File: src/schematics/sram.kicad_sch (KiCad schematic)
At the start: 4 parts, among them U9 IS61WV25616BLL-*BLI

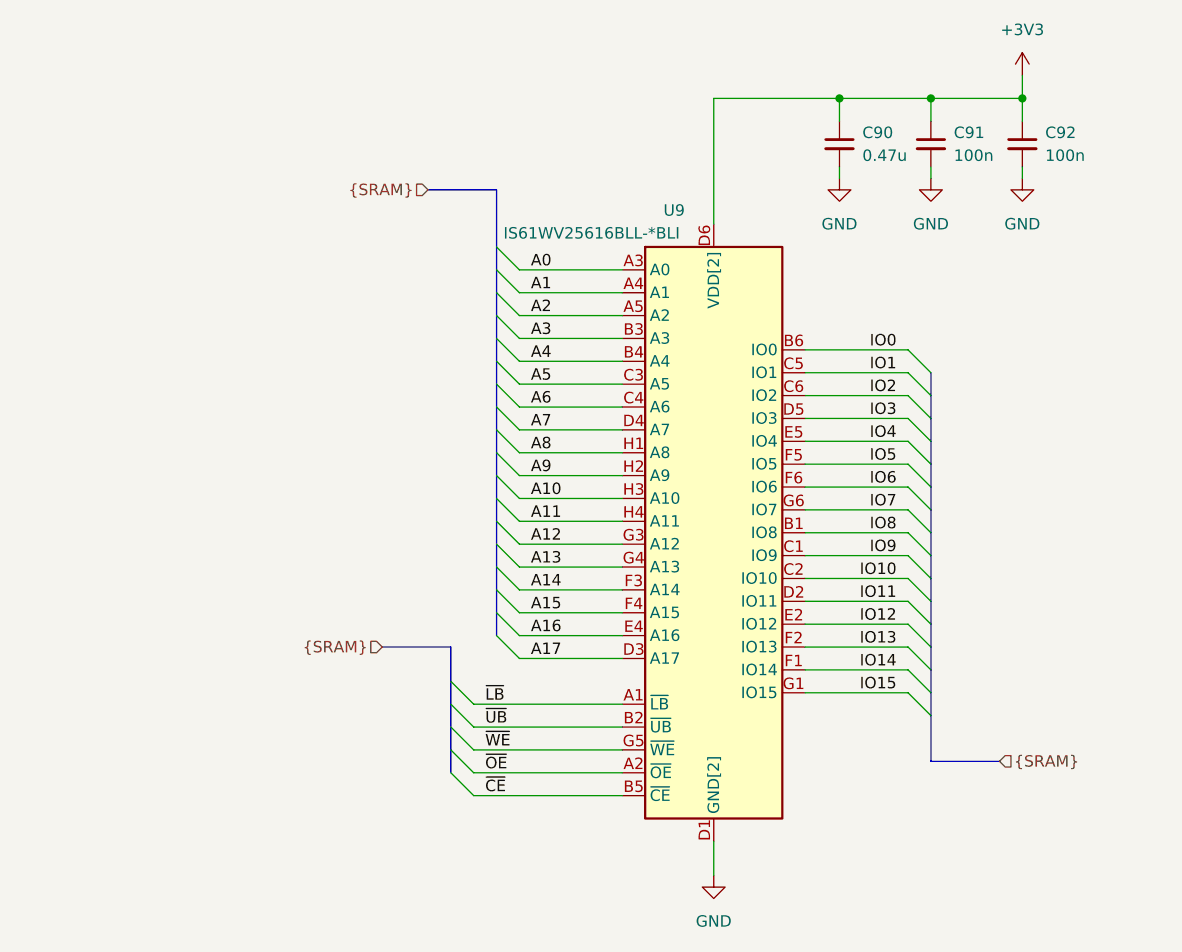
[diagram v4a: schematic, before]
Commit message: Remove bus groups
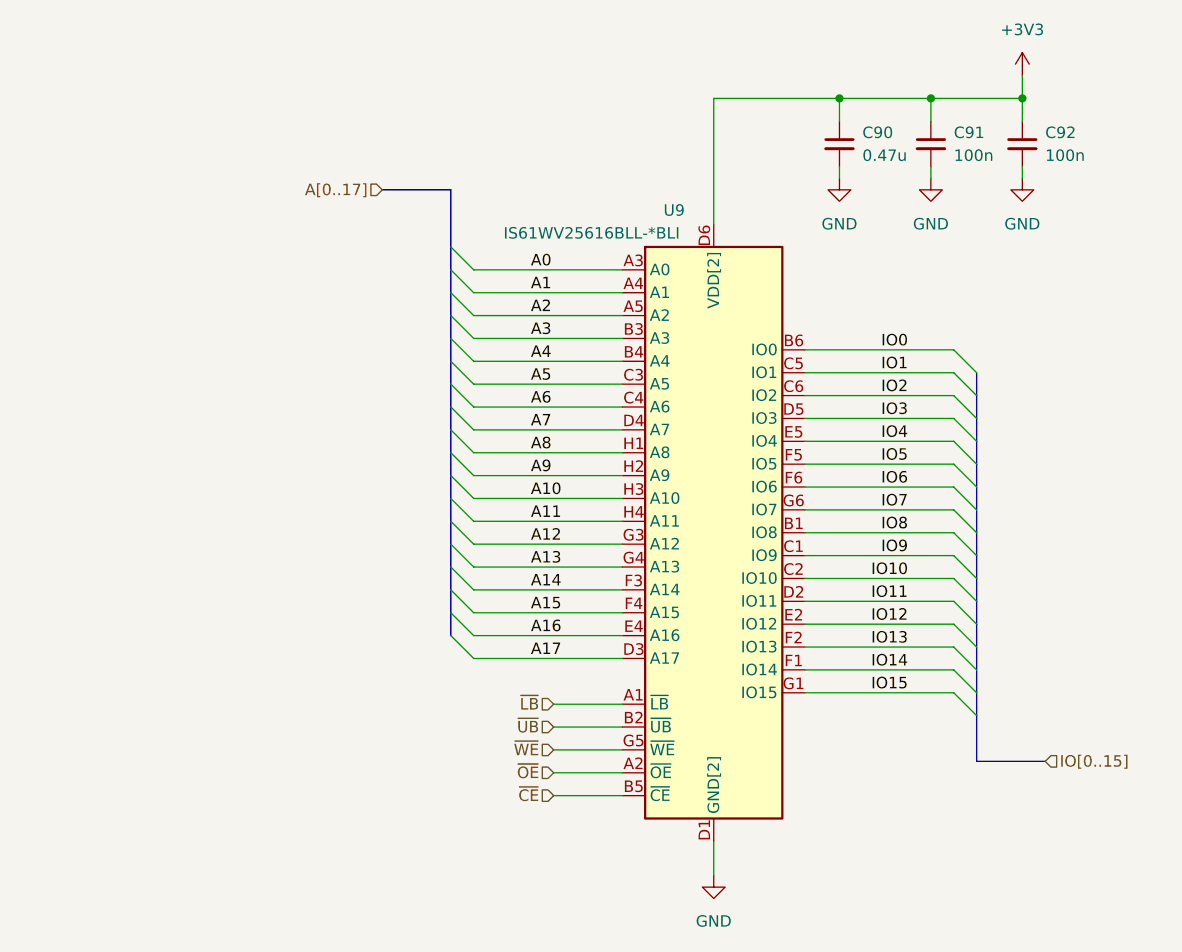
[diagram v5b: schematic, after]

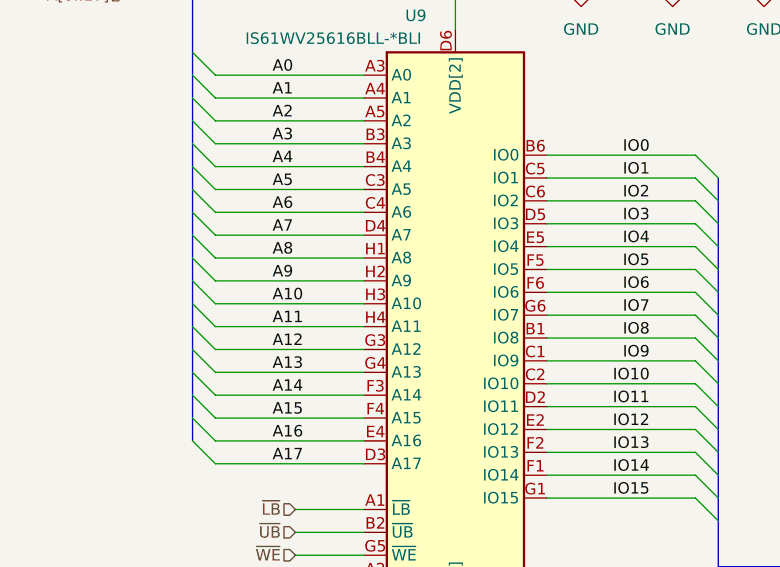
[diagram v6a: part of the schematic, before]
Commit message: ✅ Validate the SRAM symbol
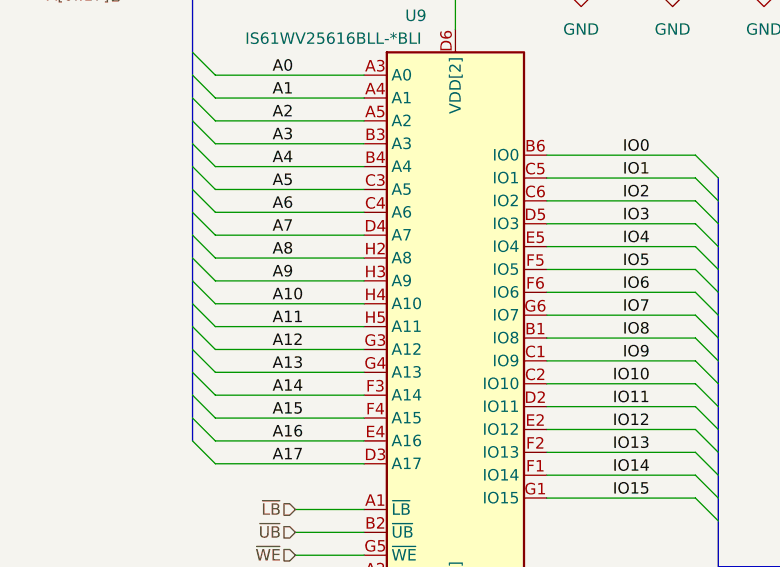
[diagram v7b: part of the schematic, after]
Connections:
- net A10: now also U9.H4 (A10); no longer U9.H3 (A10)
- net A11: now also U9.H5 (A11); no longer U9.H4 (A11)
- net A8: now also U9.H2 (A8); no longer U9.H1 (NC)
- net A9: now also U9.H3 (A9); no longer U9.H2 (A9)
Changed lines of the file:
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@@
 	(label "IO4"
 		(at 173.99 86.36 180)
-		(fields_autoplaced yes)
 		(effects
 			(font
@@
 	(label "A1"
 		(at 132.08 69.85 0)
-		(fields_autoplaced yes)
 		(effects
 			(font
@@
 	(label "IO9"
 		(at 173.99 99.06 180)
-		(fields_autoplaced yes)
 		(effects
 			(font
@@
 	(label "A10"
 		(at 132.08 92.71 0)
-		(fields_autoplaced yes)
 		(effects
 			(font
@@
 	(label "A0"
 		(at 132.08 67.31 0)
-		(fields_autoplaced yes)
 		(effects
 			(font
@@
 	(label "IO8"
 		(at 173.99 96.52 180)
-		(fields_autoplaced yes)
 		(effects
 			(font
@@
 	(label "A6"
 		(at 132.08 82.55 0)
-		(fields_autoplaced yes)
 		(effects
 			(font
@@
 	(label "A3"
 		(at 132.08 74.93 0)
-		(fields_autoplaced yes)
 		(effects
 			(font
@@
 	(label "A9"
 		(at 132.08 90.17 0)
-		(fields_autoplaced yes)
 		(effects
 			(font
@@
 	(label "A16"
 		(at 132.08 107.95 0)
-		(fields_autoplaced yes)
 		(effects
 			(font
@@
 	(label "A7"
 		(at 132.08 85.09 0)
-		(fields_autoplaced yes)
 		(effects
 			(font
@@
 	(label "IO5"
 		(at 173.99 88.9 180)
-		(fields_autoplaced yes)
 		(effects
 			(font
@@
 	(label "A8"
 		(at 132.08 87.63 0)
-		(fields_autoplaced yes)
 		(effects
 			(font
@@
 	(label "A4"
 		(at 132.08 77.47 0)
-		(fields_autoplaced yes)
 		(effects
 			(font
@@
 	(label "A11"
 		(at 132.08 95.25 0)
-		(fields_autoplaced yes)
 		(effects
 			(font
@@
 	(label "IO14"
 		(at 173.99 111.76 180)
-		(fields_autoplaced yes)
 		(effects
 			(font
@@
 	(label "A13"
 		(at 132.08 100.33 0)
-		(fields_autoplaced yes)
 		(effects
 			(font
@@
 	(label "IO0"
 		(at 173.99 76.2 180)
-		(fields_autoplaced yes)
 		(effects
 			(font
@@
 	(label "IO13"
 		(at 173.99 109.22 180)
-		(fields_autoplaced yes)
 		(effects
 			(font
@@
 	(label "A15"
 		(at 132.08 105.41 0)
-		(fields_autoplaced yes)
 		(effects
 			(font
@@
 	(label "A12"
 		(at 132.08 97.79 0)
-		(fields_autoplaced yes)
 		(effects
 			(font
@@
 	(label "IO10"
 		(at 173.99 101.6 180)
-		(fields_autoplaced yes)
 		(effects
 			(font
@@
 	(label "A17"
 		(at 132.08 110.49 0)
-		(fields_autoplaced yes)
 		(effects
 			(font
@@
 	(label "IO15"
 		(at 173.99 114.3 180)
-		(fields_autoplaced yes)
 		(effects
 			(font
@@
 	(label "A14"
 		(at 132.08 102.87 0)
-		(fields_autoplaced yes)
 		(effects
 			(font
@@
 	(label "IO1"
 		(at 173.99 78.74 180)
-		(fields_autoplaced yes)
 		(effects
 			(font
@@
 	(label "IO2"
 		(at 173.99 81.28 180)
-		(fields_autoplaced yes)
 		(effects
 			(font
@@
 	(label "IO6"
 		(at 173.99 91.44 180)
-		(fields_autoplaced yes)
 		(effects
 			(font
@@
 	(label "IO3"
 		(at 173.99 83.82 180)
-		(fields_autoplaced yes)
 		(effects
 			(font
@@
 	(label "A2"
 		(at 132.08 72.39 0)
-		(fields_autoplaced yes)
 		(effects
 			(font
@@
 	(label "A5"
 		(at 132.08 80.01 0)
-		(fields_autoplaced yes)
 		(effects
 			(font
@@
 	(label "IO12"
 		(at 173.99 106.68 180)
-		(fields_autoplaced yes)
 		(effects
 			(font
@@
 	(label "IO7"
 		(at 173.99 93.98 180)
-		(fields_autoplaced yes)
 		(effects
 			(font
@@
 	(label "IO11"
 		(at 173.99 104.14 180)
-		(fields_autoplaced yes)
 		(effects
 			(font
@@
 		(shape input)
 		(at 134.62 120.65 180)
-		(fields_autoplaced yes)
 		(effects
 			(font
@@
 		(shape input)
 		(at 134.62 115.57 180)
-		(fields_autoplaced yes)
 		(effects
 			(font
@@
 		(shape input)
 		(at 134.62 125.73 180)
-		(fields_autoplaced yes)
 		(effects
 			(font
@@
 		(shape input)
 		(at 189.23 121.92 0)
-		(fields_autoplaced yes)
 		(effects
 			(font
@@
 		(shape input)
 		(at 115.57 58.42 180)
-		(fields_autoplaced yes)
 		(effects
 			(font
@@
 		(shape input)
 		(at 134.62 118.11 180)
-		(fields_autoplaced yes)
 		(effects
 			(font
@@
 		(shape input)
 		(at 134.62 123.19 180)
-		(fields_autoplaced yes)
 		(effects
 			(font
@@
 		(pin "H6"
 		)
-		(pin "H1"
+		(pin "H5"
 		)
 		(pin "G4"
